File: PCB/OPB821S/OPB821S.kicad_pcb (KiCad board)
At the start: 2 copper layers, 21 parts, among them J1 Conn_02x02, J10 Screw_Terminal_01x02, J2 Conn_02x02, J3 Conn_01x02, J4 Conn_02x05_Counter_Clockwise, J7 LEMO5, J8 Screw_Terminal_01x03, J9 LEMO5, U1 74HC14, U2 OP249

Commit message: OPB board ended - docs produce for report
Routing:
- net /Vm: track 24.9 -> 21.2 mm
- net (no net): vias 42 -> 28
- added copper zone on B.Cu, net GND
- added copper zone on F.Cu, net GND

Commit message: add last document & convert line in class 4
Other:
- net class Default: clearance 0.2 -> 0.21
- rule trace_clearance: 0.2 -> 0.21
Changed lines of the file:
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@@
     (links 56)
     (no_connects 1)
-    (area 133.825 45.025 204.075 89.075)
+    (area 133.815 45.015 204.085 89.085)
     (thickness 1.6)
-    (drawings 4)
+    (drawings 8)
     (tracks 113)
     (zones 0)
@@
   )
   (setup
-    (last_trace_width 0.8)
+    (last_trace_width 0.25)
     (user_trace_width 0.25)
     (user_trace_width 0.5)
     (user_trace_width 0.6)
     (user_trace_width 0.8)
-    (trace_clearance 0.2)
+    (trace_clearance 0.21)
     (zone_clearance 0.508)
     (zone_45_only yes)
@@
     (aux_axis_origin 0 0)
     (grid_origin 169 65)
-    (visible_elements FFFFFFFF)
+    (visible_elements 7FFFFFFF)
     (pcbplotparams
-      (layerselection 0x20000_80000001)
+      (layerselection 0x20000_00000000)
       (usegerberextensions false)
-      (excludeedgelayer true)
+      (excludeedgelayer false)
       (linewidth 0.100000)
       (plotframeref false)
@@
       (padsonsilk true)
       (subtractmaskfromsilk false)
-      (outputformat 1)
+      (outputformat 4)
       (mirror false)
       (drillshape 0)
       (scaleselection 1)
-      (outputdirectory Fichier_GERBER/))
+      (outputdirectory Docs/))
   )
   (net 0 "")
@@
   (net 16 "Net-(J4-Pad4)")
   (net_class Default "Ceci est la Netclass par défaut"
-    (clearance 0.2)
+    (clearance 0.21)
     (trace_width 0.25)
     (via_dia 0.6)
@@
     (descr "Spindle Trimmer Potentiometer, Bourns 3296W, https://www.bourns.com/pdfs/3296.pdf")
     (tags "Spindle Trimmer Potentiometer   Bourns 3296W")
-    (fp_text reference RV1 (at 0.664 -1.532 450) (layer F.SilkS)
+    (fp_text reference RV1 (at -8.636 1.068 540) (layer F.SilkS)
       (effects (font (size 1 1) (thickness 0.15)))
     )
@@
       (effects (font (size 1 1) (thickness 0.15)) (justify mirror))
     )
-    (fp_text value 100nF (at 0.127 1.881 270) (layer B.Fab)
+    (fp_text value 100nF (at 0.127 -2.119 270) (layer B.Fab)
       (effects (font (size 1 1) (thickness 0.15)) (justify mirror))
     )
@@
     (descr "14-lead though-hole mounted DIP package, row spacing 7.62 mm (300 mils), LongPads")
     (tags "THT DIP DIL PDIP 2.54mm 7.62mm 300mil LongPads")
-    (fp_text reference U1 (at 2.992 -2.453 270) (layer F.SilkS)
+    (fp_text reference U1 (at 2.992 -2.453 360) (layer F.SilkS)
       (effects (font (size 1 1) (thickness 0.15)))
     )
@@
     (fp_line (start 9.1 16.8) (end 9.1 -1.55) (layer F.CrtYd) (width 0.05))
     (fp_line (start 9.1 -1.55) (end -1.45 -1.55) (layer F.CrtYd) (width 0.05))
-    (fp_text user %R (at 2.992 -2.453 270) (layer F.Fab)
+    (fp_text user %R (at 2.992 -2.453 360) (layer F.Fab)
       (effects (font (size 1 1) (thickness 0.15)))
     )
@@
       (effects (font (size 1 1) (thickness 0.15)) (justify mirror))
     )
-    (fp_text value 10K (at -2.826 -0.134 180) (layer B.Fab)
+    (fp_text value 10K (at 0.174 -1.634 90) (layer B.Fab)
       (effects (font (size 1 1) (thickness 0.15)) (justify mirror))
     )
@@
     )
   )
+  (gr_line (start 137 47) (end 202 47) (angle 90) (layer B.CrtYd) (width 0.2))
+  (gr_line (start 137 87) (end 137 47) (angle 90) (layer B.CrtYd) (width 0.2))
+  (gr_line (start 202 87) (end 137 87) (angle 90) (layer B.CrtYd) (width 0.2))
+  (gr_line (start 202 47) (end 202 87) (angle 90) (layer B.CrtYd) (width 0.2))
   (gr_line (start 137 87) (end 137 47) (angle 90) (layer F.Fab) (width 0.2))
   (gr_line (start 202 87) (end 137 87) (angle 90) (layer F.Fab) (width 0.2))
@@
   (segment (start 172.847 74.549) (end 174.244 75.946) (width 0.6) (layer B.Cu) (net 16))
   (zone (net 1) (net_name GND) (layer F.Cu) (hatch edge 0.508)
-    (connect_pads thru_hole_only (clearance 0.508))
+    (connect_pads (clearance 0.508))
     (min_thickness 0.254)
     (fill yes (arc_segments 16) (thermal_gap 0.508) (thermal_bridge_width 0.508))
@@
   )
   (zone (net 1) (net_name GND) (layer B.Cu) (hatch edge 0.508)
-    (connect_pads thru_hole_only (clearance 0.508))
+    (connect_pads (clearance 0.508))
     (min_thickness 0.254)
     (fill yes (arc_segments 16) (thermal_gap 0.508) (thermal_bridge_width 0.508))

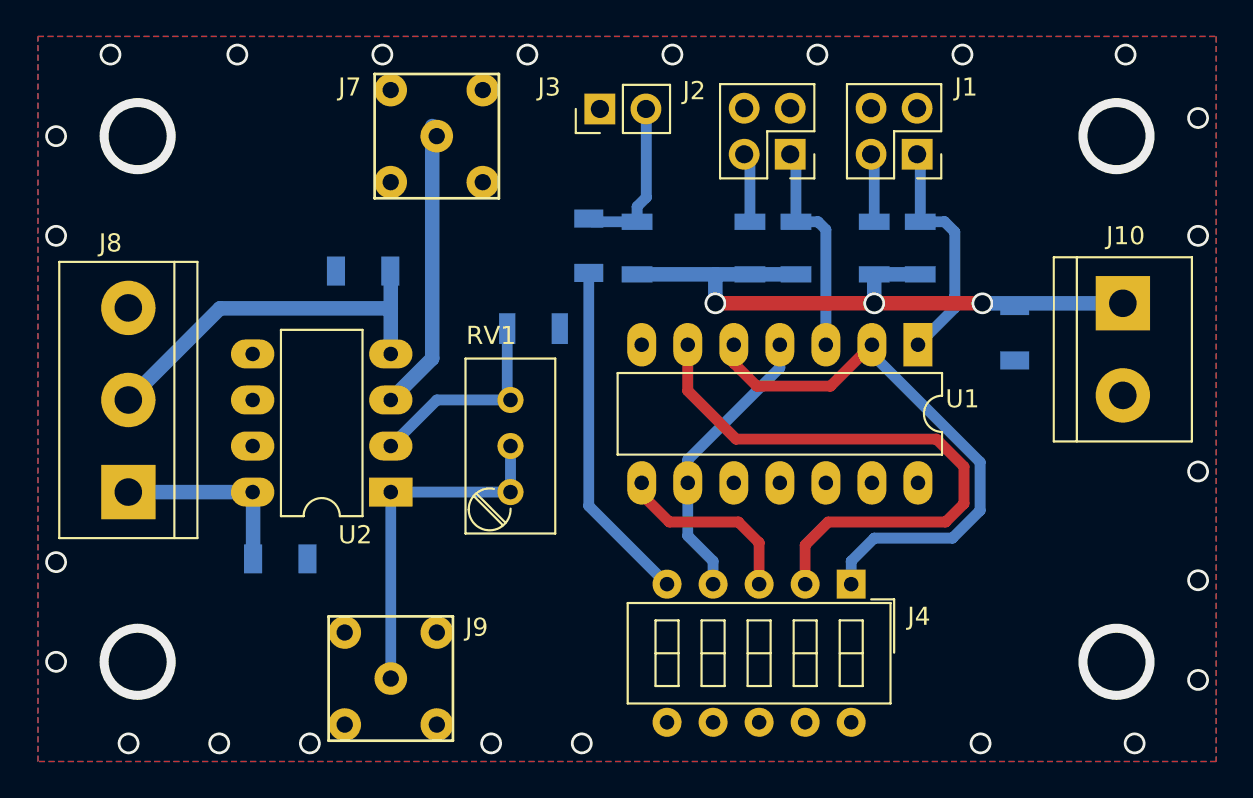
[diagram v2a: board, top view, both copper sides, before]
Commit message: fix error for photoContactor connexion
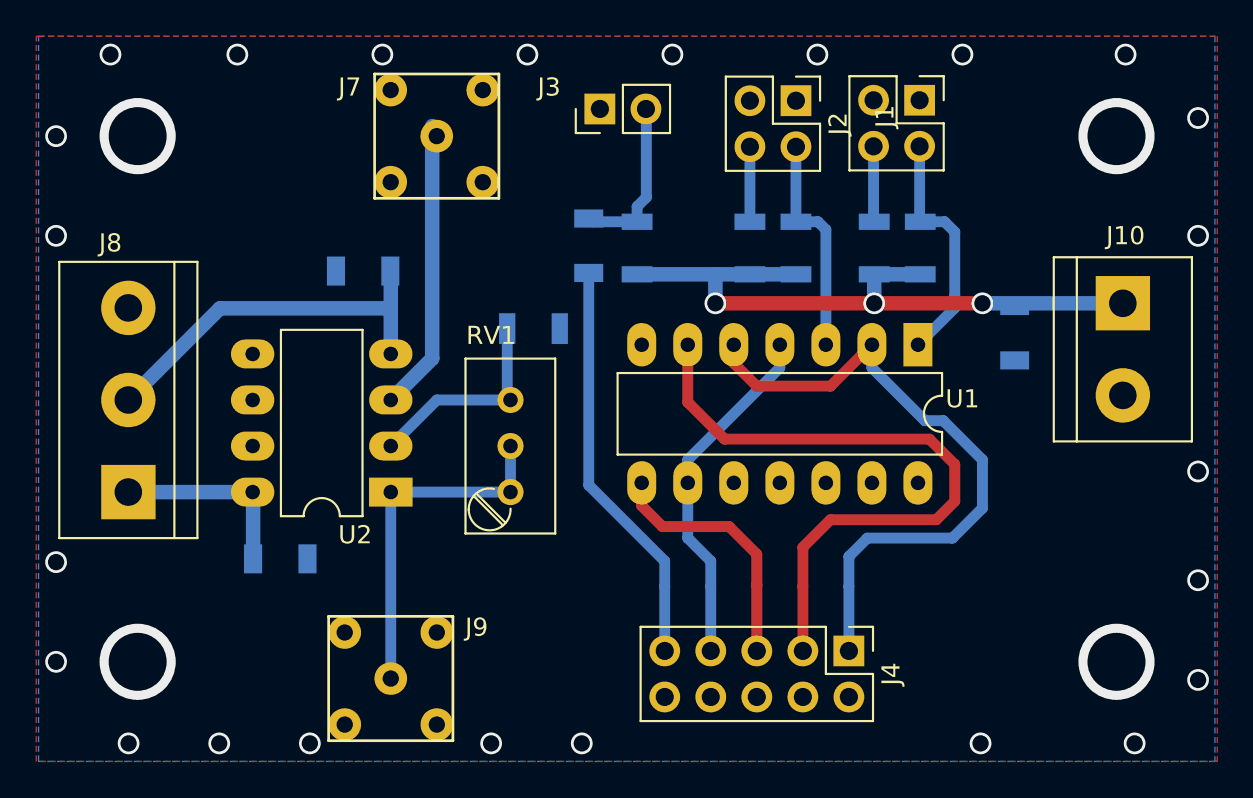
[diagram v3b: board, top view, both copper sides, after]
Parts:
- J4: value Conn_02x05_Counter_Clockwise -> Conn_02x05_Odd_Even; footprint Buttons_Switches_THT:SW_DIP_x5_W7.62mm_Slide_LowProfile -> Pin_Headers:Pin_Header_Straight_2x05_Pitch2.54mm
- moved J4 3.69 mm to (181.7, 80.9)
- moved J1 2.98 mm to (185.6, 50.5), turned to 270 degrees
- moved J2 2.97 mm to (178.8, 50.5), turned to 270 degrees
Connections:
- J1 pad 1: Net-(J1-Pad1) -> GND
- J1 pad 4: GND -> Net-(J1-Pad4)
- J2 pad 1: Net-(J2-Pad1) -> GND
- J2 pad 4: GND -> Net-(J2-Pad4)
- J4 pad 2: Net-(J4-Pad2) -> GND
- J4 pad 4: Net-(J4-Pad4) -> GND
- J4 pad 5: GND -> Net-(J4-Pad5)
- J4 pad 7: GND -> Net-(J4-Pad7)
- R2 pad 2: Net-(J1-Pad2) -> Net-(J1-Pad4)
- R3 pad 2: Net-(J1-Pad1) -> Net-(J1-Pad2)
- R4 pad 2: Net-(J2-Pad2) -> Net-(J2-Pad4)
- R5 pad 2: Net-(J2-Pad1) -> Net-(J2-Pad2)
- U1 pad 1: Net-(J1-Pad1) -> Net-(J1-Pad2)
- U1 pad 3: Net-(J2-Pad1) -> Net-(J2-Pad2)
- U1 pad 4: Net-(J4-Pad4) -> Net-(J4-Pad7)
- U1 pad 6: Net-(J4-Pad2) -> Net-(J4-Pad3)
- U1 pad 8: Net-(J4-Pad3) -> Net-(J4-Pad5)
- U1 pad 9: Net-(J4-Pad4) -> Net-(J4-Pad7)
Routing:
- net Net-(J4-Pad2): track 33.4 -> 0.00 mm
- net Net-(J4-Pad3): track 10.5 -> 36.5 mm
- net Net-(J4-Pad7): track 0.00 -> 19.5 mm
- net Net-(J4-Pad4): track 15.9 -> 0.00 mm
- net Net-(J4-Pad5): track 0.00 -> 14.2 mm
- net Net-(J1-Pad1): track 13.3 -> 0.00 mm
- net Net-(J2-Pad1): track 12.5 -> 0.00 mm
- net Net-(J1-Pad2): track 4.14 -> 13.4 mm
- net Net-(J2-Pad2): track 4.14 -> 12.5 mm
- net Net-(J4-Pad1): track 31.3 -> 35.9 mm
- net Net-(J1-Pad4): track 0.00 -> 4.18 mm
- net Net-(J2-Pad4): track 0.00 -> 4.14 mm
- net GND: track 19.0 -> 22.6 mm

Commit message: Update - prototype tested and fonctional
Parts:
- R3, R5: value 10K -> 100
- moved C4 3.24 mm to (191.1, 60.1), turned to 90 degrees
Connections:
- C4 pad 1: /Vopb -> VCC
- J10 pad 1: /Vopb -> VCC
- R1 pad 2: /Vopb -> VCC
- R2 pad 1: /Vopb -> VCC
- R3 pad 1: /Vopb -> VCC
- R4 pad 1: /Vopb -> VCC
- R5 pad 1: /Vopb -> VCC
- U1 pad 14: (no net) -> VCC
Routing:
- net VCC: track 0.00 -> 51.8 mm, vias 0 -> 3
- net /Vopb: track 37.1 -> 0.00 mm, vias 3 -> 0
- net Net-(J4-Pad1): track 35.9 -> 39.8 mm, vias 0 -> 2
